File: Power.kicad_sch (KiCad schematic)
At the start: 69 parts, among them U2001 TPSM861253RDXR, U2003 TPS546D24S, U2004 TPS546D24S

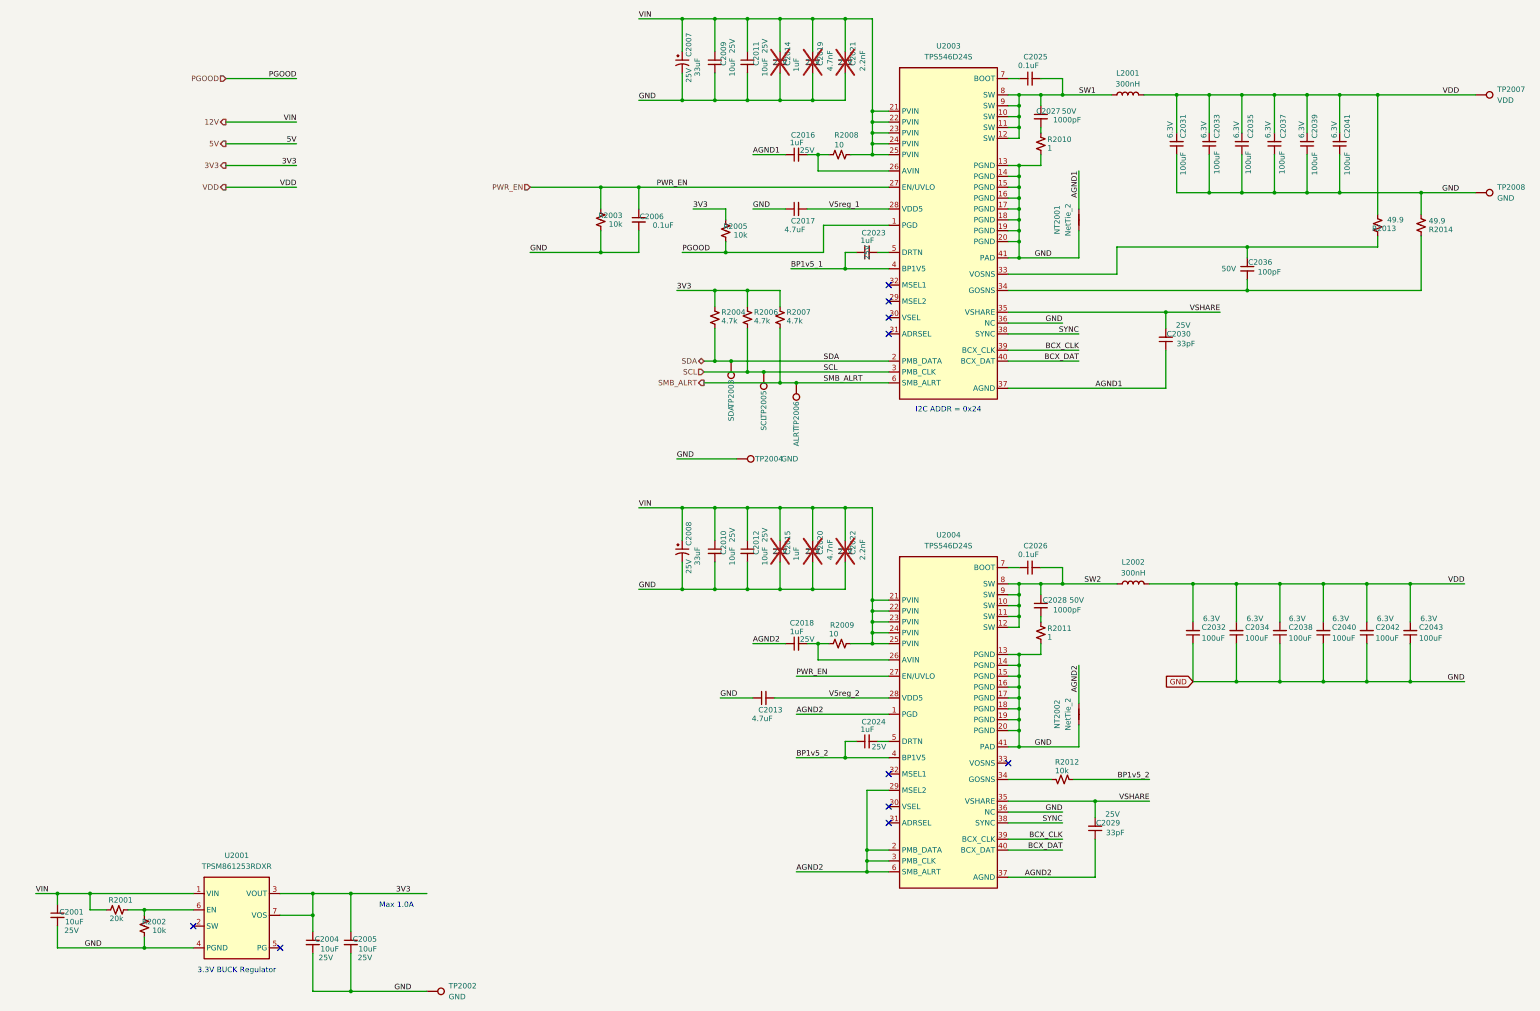
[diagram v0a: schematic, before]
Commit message: finished adding ASICs to schematic. Change VR to single phase 2.8V output
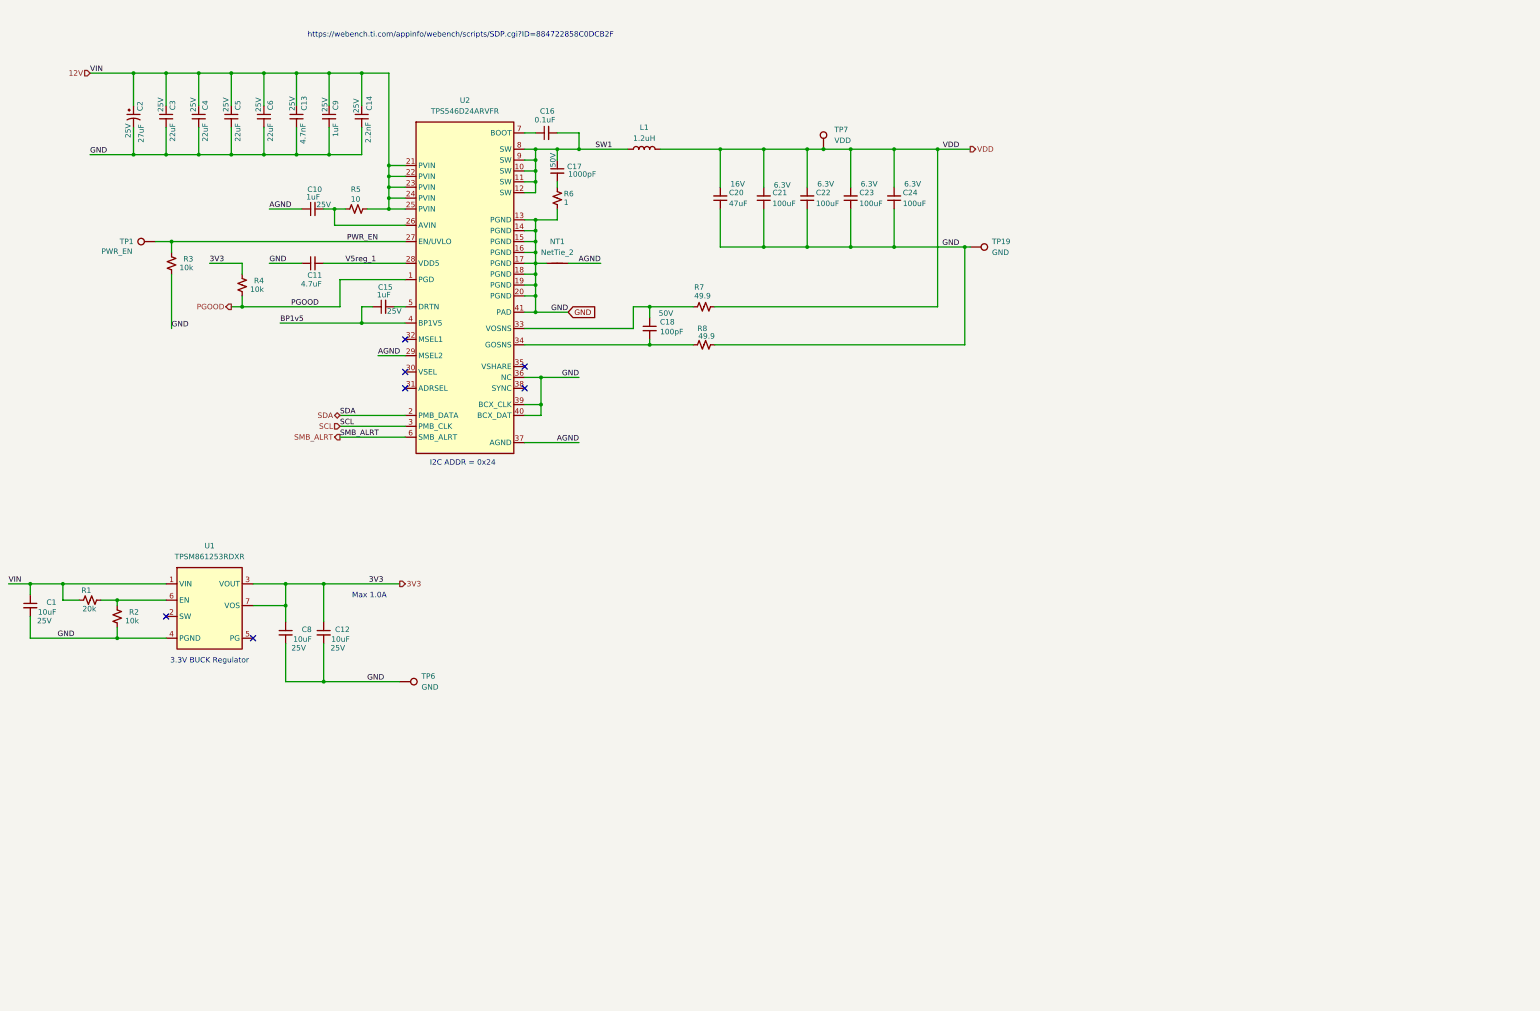
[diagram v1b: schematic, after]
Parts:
- removed C2006, C2026: 0.1uF, Capacitor_SMD:C_0402_1005Metric, symbol Device:C_Small
- removed C2008: 33uF, Capacitor_Tantalum_SMD:CP_EIA-7343-31_Kemet-D, symbol Device:C_Polarized_Small_US
- removed C2009, C2010, C2011, C2012: 10uF, Capacitor_SMD:C_0603_1608Metric, symbol Device:C_Small
- removed C2013: 4.7uF, Capacitor_SMD:C_0402_1005Metric, symbol Device:C_Small
- removed C2015, C2018, C2024: 1uF, Capacitor_SMD:C_0402_1005Metric, symbol Device:C_Small
- removed C2020: 4.7nF, Capacitor_SMD:C_0402_1005Metric, symbol Device:C_Small
- removed C2022: 2.2nF, Capacitor_SMD:C_0402_1005Metric, symbol Device:C_Small
- removed C2028: 1000pF, Capacitor_SMD:C_0805_2012Metric, symbol Device:C_Small
- removed C2029, C2030: 33pF, Capacitor_SMD:C_0402_1005Metric, symbol Device:C_Small
- removed C2031, C2032, C2034, C2038, C2040, C2042, C2043: 100uF, Capacitor_SMD:C_1206_3216Metric, symbol Device:C_Small
- removed L2002: 300nH, bitaxe:SLC1175-271MEC_COC, symbol Device:L
- removed NT2002: NetTie_2, bitaxe:NetTie-2_SMD_Pad0.2mmx1mm, symbol Device:NetTie_2
- removed R2003, R2012: 10k, Resistor_SMD:R_0402_1005Metric, symbol Device:R_Small_US
- removed R2004, R2006, R2007: 4.7k, Resistor_SMD:R_0402_1005Metric, symbol Device:R_Small_US
- removed R2009: 10, Resistor_SMD:R_0402_1005Metric, symbol Device:R_Small_US
- removed R2011: 1, Resistor_SMD:R_0805_2012Metric, symbol Device:R_Small_US
- removed TP2003: SDA, bitaxe:TestPoint_Pad_D1.0mm, symbol Connector:TestPoint
- removed TP2004: GND, bitaxe:TestPoint_Pad_D1.0mm, symbol Connector:TestPoint
- removed TP2005: SCL, bitaxe:TestPoint_Pad_D1.0mm, symbol Connector:TestPoint
- removed TP2006: ALRT, bitaxe:TestPoint_Pad_D1.0mm, symbol Connector:TestPoint
- removed U2004: TPS546D24S, bitaxe:LQFN40-CLIP, symbol bitaxe:TPS546D24
- added C3, C4, C5, C6: 22uF, Capacitor_SMD:C_1210_3225Metric, symbol Device:C_Small
- added R3: 10k, Resistor_SMD:R_0402_1005Metric, symbol Device:R_Small_US
- added TP1: PWR_EN, TestPoint:TestPoint_Pad_D1.0mm, symbol Connector:TestPoint
- C13: renamed from C2019; now fitted; now in the parts list
- C14: renamed from C2021; now fitted; now in the parts list
- C2: renamed from C2007; value 33uF -> 27uF; footprint Capacitor_Tantalum_SMD:CP_EIA-7343-31_Kemet-D -> Capacitor_SMD:CP_Elec_5x5.9; DK 399-3882-1-ND -> 565-APXG250ARA270MF46GCT-ND; PARTNO T495D336K025ATE300 -> APXG250ARA270MF46G
- C20: renamed from C2033; value 100uF -> 47uF; footprint Capacitor_SMD:C_1206_3216Metric -> Capacitor_SMD:C_1210_3225Metric; DK 1276-1782-1-ND -> (none); PARTNO CL31A107MQHNNNE -> GRM32ER61C476KE15L; Voltage 6.3V -> 16V
- C9: renamed from C2014; now fitted; now in the parts list
- L1: renamed from L2001; value 300nH -> 1.2uH; footprint bitaxe:SLC1175-271MEC_COC -> bitaxe:XAL1060122MEC; DK (none) -> 2457-XAL1060-122MEC-ND; PARTNO SLC1175-271MEC -> XAL1060-122MEC
- TP19: renamed from TP2008; footprint bitaxe:TestPoint_Pad_D1.0mm -> TestPoint:TestPoint_Pad_D1.0mm
- TP7: renamed from TP2007; footprint bitaxe:TestPoint_Pad_D1.0mm -> TestPoint:TestPoint_Pad_D1.0mm
- U2: renamed from U2003; value TPS546D24S -> TPS546D24ARVFR; DK 296-TPS546D24SRVFRCT-ND -> 296-TPS546D24ARVFRCT-ND; PARTNO TPS546D24SRVFR -> TPS546D24ARVFR
- renumbered C2001 to C1, C2016 to C10, C2017 to C11, C2005 to C12, C2023 to C15, C2025 to C16, C2027 to C17, C2036 to C18, C2035 to C21, C2037 to C22, C2039 to C23, C2041 to C24, C2004 to C8, NT2001 to NT1, R2001 to R1, R2002 to R2, R2005 to R4, R2008 to R5, R2010 to R6, R2013 to R7, R2014 to R8, TP2002 to TP6, U2001 to U1
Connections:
- net AGND1 is gone; now on net AGND: C10.1, NT1.2, U2.37 (AGND)
- net BCX_CLK is gone; now on net GND: U2.39 (BCX_CLK)
- net BCX_DAT is gone; now on net GND: U2.40 (BCX_DAT)
- net 12V: now also C3.1, C4.1, C5.1, C6.1
- net GND: now also R8.2, C3.2, C4.2, C5.2, C6.2, R3.1; no longer R8.1
- net PWR_EN: now also R3.2, TP1.1
- net VDD: now also R7.1; no longer R7.2
- net at C18.2, U2.34 (GOSNS): now also R8.1; no longer R8.2
- net at C18.1, U2.33 (VOSNS): now also R7.2; no longer R7.1
- net AGND: now reaches U2.29 (MSEL2)
- net BP1v5_1 renamed BP1v5
- net SYNC: no longer names the net of U2.38 (SYNC)
- net VSHARE: no longer names the net of U2.35 (VSHARE)
- no-connect marks 10 -> 7
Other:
- note added: "https://webench.ti.com/appinfo/webench/scripts/SDP.cgi?ID=884722858C0DCB2F"
- moved on the sheet: C1, C10, C11, C12, C15, C16, C17, C18, C2, C20, C21, C22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

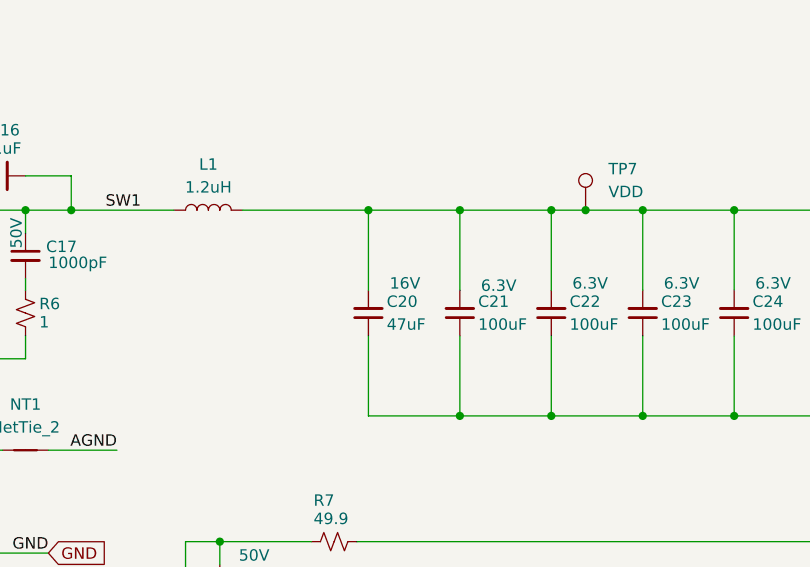
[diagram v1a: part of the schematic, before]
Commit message: switched to smaller level shifter diodes. switched ASIC modes
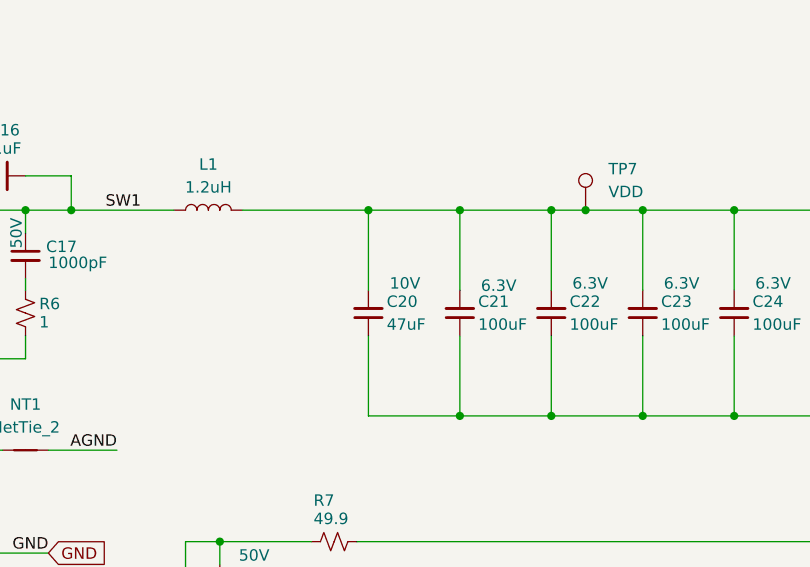
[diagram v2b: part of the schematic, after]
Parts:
- C20: footprint Capacitor_SMD:C_1210_3225Metric -> Capacitor_SMD:C_1206_3216Metric; DK (none) -> 490-5528-1-ND; PARTNO GRM32ER61C476KE15L -> GRM31CR61A476ME15L; Voltage 16V -> 10V
- C3, C4, C5, C6: footprint Capacitor_SMD:C_1210_3225Metric -> Capacitor_SMD:C_1206_3216Metric; DK (none) -> 587-3246-1-ND; PARTNO GRM32ER61E226KE15L -> TMK316BBJ226ML-T
- TP1, TP19, TP7: footprint TestPoint:TestPoint_Pad_D1.0mm -> bitaxe:TestPoint_Pad_D1.0mm

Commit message: more routing
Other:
- moved on the sheet: TP1
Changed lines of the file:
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@@
 	)
 	(junction
+		(at 85.09 72.39)
+		(diameter 0)
+		(color 0 0 0 0)
+	)
+	(junction
 		(at 121.92 59.69)
 		(diameter 0)
@@
 	(wire
 		(pts
-			(xy 71.12 72.39) (xy 125.73 72.39)
+			(xy 71.12 72.39) (xy 85.09 72.39)
 		)
 		(stroke
@@
 		)
 	)
+	(wire
+		(pts
+			(xy 85.09 72.39) (xy 125.73 72.39)
+		)
+		(stroke
+			(width 0)
+			(type default)
+		)
+	)
 	(label "GND"
 		(at 71.12 92.71 0)
@@
 		)
 	)
+	(hierarchical_label "PWR_EN"
+		(shape input)
+		(at 67.31 72.39 180)
+		(effects
+			(font
+				(size 1.27 1.27)
+			)
+			(justify right)
+		)
+	)
 	(hierarchical_label "SMB_ALRT"
 		(shape output)
@@
 	(symbol
 		(lib_id "Connector:TestPoint")
-		(at 67.31 72.39 90)
-		(mirror x)
+		(at 85.09 72.39 0)
+		(mirror y)
 		(unit 1)
 		(exclude_from_sim no)
@@
 		(dnp no)
 		(property "Reference" "TP1"
-			(at 62.23 72.39 90)
+			(at 85.09 67.31 90)
 			(effects
 				(font
@@
 		)
 		(property "Value" "PWR_EN"
-			(at 61.976 74.676 90)
+			(at 82.804 67.056 90)
 			(effects
 				(font
@@
 		)
 		(property "Footprint" "bitaxe:TestPoint_Pad_D1.0mm"
-			(at 67.31 77.47 0)
+			(at 80.01 72.39 0)
 			(effects
 				(font
@@
 		)
 		(property "Datasheet" "~"
-			(at 67.31 77.47 0)
+			(at 80.01 72.39 0)
 			(effects
 				(font
@@
 		)
 		(property "Description" "test point"
-			(at 67.31 72.39 0)
+			(at 85.09 72.39 0)
 			(effects
 				(font
@@
 		)
 		(property "Mouser" ""
-			(at 67.31 72.39 90)
+			(at 85.09 72.39 90)
 			(effects
 				(font

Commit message: Added RP Pico W2 to schematic. Fixed Domain 1-2 level shifter pins. Added test points
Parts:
- removed C1, C12, C8: 10uF, Capacitor_SMD:C_0603_1608Metric, symbol Device:C_Small
- removed R1: 20k, Resistor_SMD:R_0402_1005Metric, symbol Device:R_Small_US
- removed R2, R4: 10k, Resistor_SMD:R_0402_1005Metric, symbol Device:R_Small_US
- removed TP6: GND, bitaxe:TestPoint_Pad_D1.0mm, symbol Connector:TestPoint
- removed U1: TPSM861253RDXR, bitaxe:TPSM863257RDX, symbol bitaxe:TPSM861253RDXR
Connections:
- no-connect marks 7 -> 5
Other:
- note removed: "3.3V BUCK Regulator"
- note removed: "Max 1.0A"

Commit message: Removed EMC2103, added discrete fan control, DRC pass, fixed logo.
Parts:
- TP1: value PWR_EN -> PWR EN
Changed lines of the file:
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@@
 			)
 		)
-		(property "Value" "PWR_EN"
+		(property "Value" "PWR EN"
 			(at 82.804 67.056 90)
 			(effects

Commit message: update TPS546D24 to `S` variant. Add render and readme.
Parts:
- U2: value TPS546D24ARVFR -> TPS546D24SRVFR; DK 296-TPS546D24ARVFRCT-ND -> 296-TPS546D24SRVFRCT-ND; PARTNO TPS546D24ARVFR -> TPS546D24SRVFR
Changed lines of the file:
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@@
 			)
 		)
-		(property "Value" "TPS546D24ARVFR"
+		(property "Value" "TPS546D24SRVFR"
 			(at 139.7 41.91 0)
 			(effects
@@
 			)
 		)
-		(property "Datasheet" "https://www.ti.com/lit/ds/symlink/tps546d24a.pdf"
+		(property "Datasheet" "https://www.ti.com/lit/ds/symlink/tps546d24s.pdf"
 			(at 139.7 46.99 0)
 			(effects
@@
 			)
 		)
-		(property "DK" "296-TPS546D24ARVFRCT-ND"
+		(property "DK" "296-TPS546D24SRVFRCT-ND"
 			(at 139.7 44.45 0)
 			(effects
@@
 			)
 		)
-		(property "PARTNO" "TPS546D24ARVFR"
+		(property "PARTNO" "TPS546D24SRVFR"
 			(at 139.7 41.91 0)
 			(effects

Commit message: update C9 and C10 to the correct 0603 footprint. Change C15 part number to be 0402
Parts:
- C10, C9: footprint Capacitor_SMD:C_0402_1005Metric -> Capacitor_SMD:C_0603_1608Metric
- C14: PARTNO 490-8257-1-ND -> GRM155R61H222KA01D
- C15: DK 587-2984-1-ND -> 587-5514-1-ND; PARTNO TMK107B7105KA-T -> EMK105BJ105MV-F; Voltage 25V -> (none)
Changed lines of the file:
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@@
 			)
 		)
-		(property "PARTNO" "TMK107B7105KA-T"
+		(property "PARTNO" "EMK105BJ105MV-F"
 			(at 120.65 87.63 90)
 			(effects
@@
 			)
 		)
-		(property "DK" "587-2984-1-ND"
+		(property "DK" "587-5514-1-ND"
 			(at 120.65 87.63 90)
 			(effects
@@
 			)
 		)
-		(property "Voltage" "25V"
+		(property "Voltage" ""
 			(at 123.19 88.646 90)
 			(effects
@@
 			)
 		)
-		(property "Footprint" "Capacitor_SMD:C_0402_1005Metric"
+		(property "Footprint" "Capacitor_SMD:C_0603_1608Metric"
 			(at 104.14 64.77 0)
 			(effects
@@
 			)
 		)
-		(property "PARTNO" "490-8257-1-ND"
+		(property "PARTNO" "GRM155R61H222KA01D"
 			(at 115.57 43.18 90)
 			(effects
@@
 			)
 		)
-		(property "Footprint" "Capacitor_SMD:C_0402_1005Metric"
+		(property "Footprint" "Capacitor_SMD:C_0603_1608Metric"
 			(at 107.95 43.18 0)
 			(effects
